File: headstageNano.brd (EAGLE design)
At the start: 15.3 x 15.4 mm, 8 parts, among them U1 RHD2132_QFN

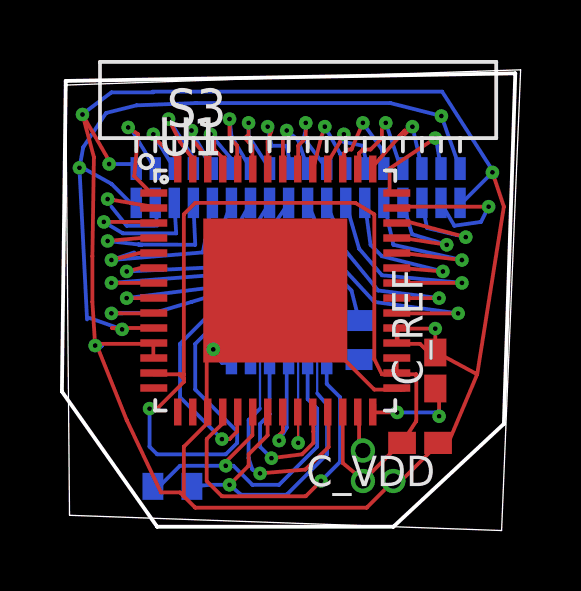
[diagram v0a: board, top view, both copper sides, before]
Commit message: ungrounded pin 33 elec_test for impedance tests
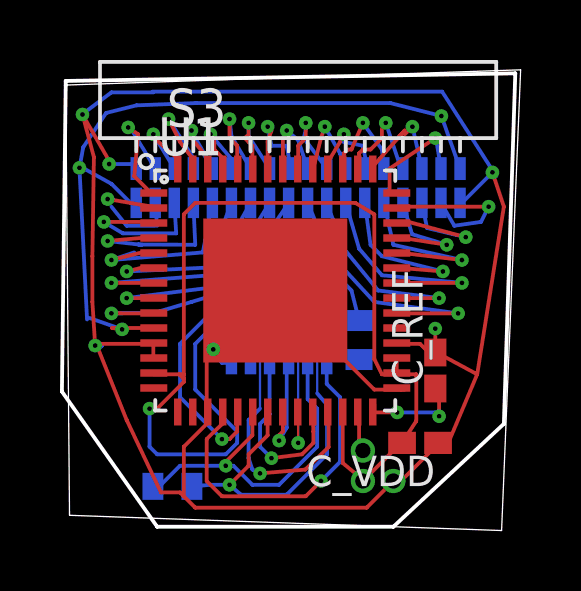
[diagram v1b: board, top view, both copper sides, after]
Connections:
- net GND: no longer U1.33
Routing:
- net GND: track 72.8 -> 70.5 mm
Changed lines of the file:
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@@
 <wire x1="25.146" y1="22.86" x2="23.3426" y2="25.6794" width="0.127" layer="16"/>
 <wire x1="23.3426" y1="25.6794" x2="13.6906" y2="25.6794" width="0.127" layer="16"/>
-<contactref element="U1" pad="33"/>
 <via x="11.3538" y="24.9174" extent="1-16" drill="0.1524"/>
 <wire x1="16.3195" y1="16.637" x2="16.002" y2="16.637" width="0.127" layer="16"/>
@@
 <wire x1="22.606" y1="17.272" x2="21.858" y2="17.272" width="0.127" layer="1"/>
 <wire x1="21.858" y1="17.272" x2="21.83" y2="17.3" width="0.127" layer="1"/>
-<wire x1="21.83" y1="17.8" x2="21.83" y2="17.3" width="0.127" layer="1"/>
 <wire x1="21.83" y1="15.8" x2="21.919" y2="15.8" width="0.127" layer="1"/>
 <wire x1="21.919" y1="15.8" x2="21.971" y2="15.748" width="0.127" layer="1"/>
-<wire x1="21.858" y1="17.272" x2="21.858" y2="17.766" width="0.127" layer="1"/>
+<wire x1="21.858" y1="17.272" x2="21.858" y2="17.766" width="0" layer="19" extent="1-16"/>
 <wire x1="21.858" y1="17.766" x2="21.844" y2="17.78" width="0.127" layer="1"/>
-<wire x1="21.844" y1="17.78" x2="23.114" y2="17.78" width="0.127" layer="1"/>
+<wire x1="21.844" y1="17.78" x2="23.114" y2="17.78" width="0" layer="19" extent="1-16"/>
 <via x="23.114" y="17.78" extent="1-16" drill="0.1524"/>
 <wire x1="23.114" y1="17.653" x2="23.114" y2="16.891" width="0.127" layer="1"/>
@@
 <wire x1="11.684" y1="18.669" x2="11.776" y2="17.215" width="0.127" layer="1"/>
 <via x="12.2428" y="23.2664" extent="1-16" drill="0.1524"/>
-<wire x1="11.811" y1="17.272" x2="11.811" y2="17.78" width="0" layer="19" extent="1-16"/>
-<wire x1="11.811" y1="17.78" x2="12.446" y2="18.415" width="0" layer="19" extent="1-16"/>
 <wire x1="11.7348" y1="23.495" x2="11.684" y2="20.193" width="0.127" layer="1"/>
 <wire x1="11.3538" y1="24.9174" x2="12.319" y2="23.241" width="0.127" layer="1"/>
@@
 <wire x1="25.019" y1="22.987" x2="23.9395" y2="21.971" width="0" layer="19" extent="1-16"/>
 <wire x1="13.73" y1="17.3" x2="13.716" y2="17.272" width="0" layer="19" extent="1-1"/>
+<wire x1="11.776" y1="17.215" x2="11.811" y2="17.272" width="0" layer="19" extent="1-16"/>
 <wire x1="23.114" y1="16.891" x2="23.114" y2="16.983" width="0" layer="19" extent="1-1"/>
+<wire x1="12.2428" y1="23.2664" x2="12.319" y2="23.241" width="0" layer="19" extent="1-1"/>
 <wire x1="25.146" y1="22.86" x2="25.019" y2="22.987" width="0" layer="19" extent="1-16"/>
-<wire x1="11.938" y1="17.145" x2="11.811" y2="17.272" width="0" layer="19" extent="1-16"/>
-<wire x1="12.2428" y1="23.2664" x2="12.319" y2="23.241" width="0" layer="19" extent="1-1"/>
 <wire x1="17.78" y1="19.05" x2="17.78" y2="18.542" width="0" layer="19" extent="1-1"/>
 <wire x1="21.83" y1="15.8" x2="21.858" y2="17.272" width="0" layer="19" extent="1-1"/>

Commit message: updating capacitor values
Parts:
- C_REF: value 0.1uF -> 10 nF
- C_VDD: value 10uF -> 100 nF
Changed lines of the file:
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@@
 <layer number="19" name="Unrouted" color="12" fill="1" visible="no" active="yes"/>
 <layer number="20" name="Dimension" color="15" fill="1" visible="yes" active="yes"/>
-<layer number="21" name="tPlace" color="7" fill="1" visible="no" active="yes"/>
-<layer number="22" name="bPlace" color="7" fill="1" visible="no" active="yes"/>
+<layer number="21" name="tPlace" color="7" fill="1" visible="yes" active="yes"/>
+<layer number="22" name="bPlace" color="7" fill="1" visible="yes" active="yes"/>
 <layer number="23" name="tOrigins" color="15" fill="1" visible="yes" active="yes"/>
 <layer number="24" name="bOrigins" color="15" fill="1" visible="yes" active="yes"/>
-<layer number="25" name="tNames" color="7" fill="1" visible="no" active="yes"/>
-<layer number="26" name="bNames" color="7" fill="1" visible="no" active="yes"/>
-<layer number="27" name="tValues" color="7" fill="1" visible="no" active="yes"/>
-<layer number="28" name="bValues" color="7" fill="1" visible="no" active="yes"/>
+<layer number="25" name="tNames" color="7" fill="1" visible="yes" active="yes"/>
+<layer number="26" name="bNames" color="7" fill="1" visible="yes" active="yes"/>
+<layer number="27" name="tValues" color="7" fill="1" visible="yes" active="yes"/>
+<layer number="28" name="bValues" color="7" fill="1" visible="yes" active="yes"/>
 <layer number="29" name="tStop" color="7" fill="3" visible="no" active="yes"/>
 <layer number="30" name="bStop" color="7" fill="6" visible="no" active="yes"/>
@@
 <element name="R2" library="resistor" package="R0402" value="100" x="14.351" y="12.5222" rot="MR180"/>
 <element name="R3" library="resistor" package="R0402" value="100" x="18.415" y="19.177" rot="MR180"/>
-<element name="C_VDD" library="resistor" package="C0402K" value="10uF" x="22.606" y="13.97" rot="R180"/>
-<element name="C_REF" library="resistor" package="C0402K" value="0.1uF" x="23.114" y="16.383" rot="R90"/>
+<element name="C_VDD" library="resistor" package="C0402K" value="100 nF" x="22.606" y="13.97" rot="R180"/>
+<element name="C_REF" library="resistor" package="C0402K" value="10 nF" x="23.114" y="16.383" rot="R90"/>
 <element name="S3" library="RHD2000b" package="OMNETICS_A79025" value="OMNETICS_A79025" x="18.542" y="24.13"/>
 </elements>
